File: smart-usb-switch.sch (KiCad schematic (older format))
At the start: 8 parts, among them J1 USB_A, J2 USB_A, J3 Conn_01x04, J4 Conn_01x02, Q1 2N7002E, U1 ESP-12F, U2 TLV75533PDBV

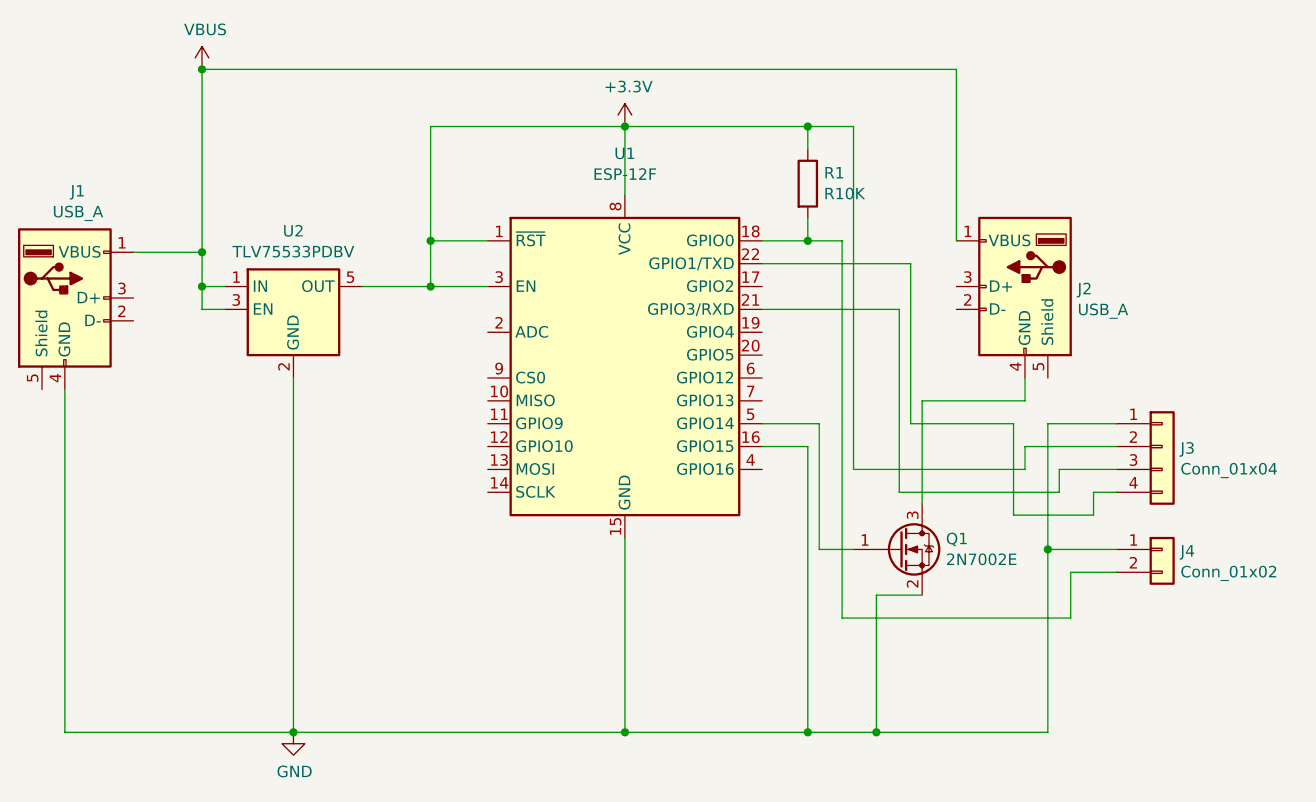
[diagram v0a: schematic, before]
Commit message: Fix #1: switch to GPIO4
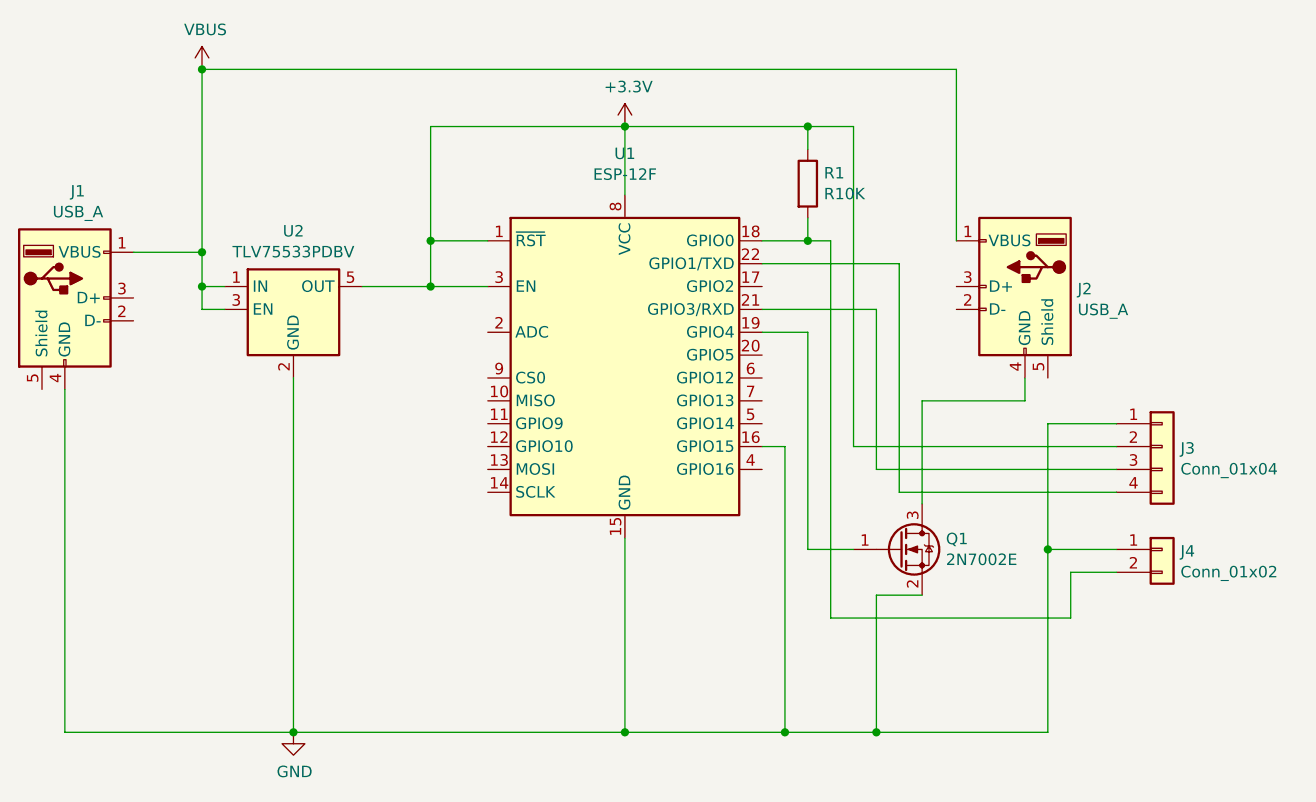
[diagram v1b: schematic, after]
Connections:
- net at U1.19 (GPIO4): now also Q1.1 (G)
- net at U1.5 (GPIO14): no longer Q1.1 (G)
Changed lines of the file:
@@
 EESchema Schematic File Version 4
-EELAYER 30 0
+EELAYER 26 0
 EELAYER END
 $Descr A4 11693 8268
@@
 Connection ~ 6800 4750
 Wire Wire Line
-	6800 4750 6500 4750
+	6800 4750 6400 4750
 Wire Wire Line
 	6800 4750 7550 4750
@@
 $EndComp
 Wire Wire Line
-	6950 3400 6950 2700
-Wire Wire Line
-	6950 2700 6300 2700
-Wire Wire Line
-	6300 2900 6900 2900
-Wire Wire Line
-	6700 3600 6700 2100
+	6900 3700 6900 2700
+Wire Wire Line
+	6900 2700 6300 2700
+Wire Wire Line
+	6300 2900 6800 2900
 Wire Wire Line
 	6700 2100 6500 2100
@@
 	7550 3400 7550 3950
 Wire Wire Line
-	7850 3500 7450 3500
-Wire Wire Line
-	7450 3500 7450 3600
-Wire Wire Line
-	7450 3600 6700 3600
-Wire Wire Line
-	7850 3600 7600 3600
-Wire Wire Line
-	7600 3600 7600 3700
-Wire Wire Line
-	7600 3700 6900 3700
-Wire Wire Line
-	6900 2900 6900 3700
-Wire Wire Line
-	6950 3400 7400 3400
-Wire Wire Line
-	7400 3400 7400 3800
-Wire Wire Line
-	7400 3800 7750 3800
-Wire Wire Line
-	7750 3800 7750 3700
-Wire Wire Line
-	7750 3700 7850 3700
+	6800 2900 6800 3600
 $Comp
 L Connector_Generic:Conn_01x02 J4
@@
 	6300 2600 6500 2600
 Wire Wire Line
-	6650 2600 6650 4250
+	6600 2600 6600 4250
 Wire Wire Line
 	7850 4050 7650 4050
 Wire Wire Line
-	6700 3950 6550 3950
-Wire Wire Line
-	6650 4250 7650 4250
+	6700 3950 6500 3950
+Wire Wire Line
+	6600 4250 7650 4250
 Wire Wire Line
 	7650 4250 7650 4050
@@
 	4250 3200 4250 4750
 Connection ~ 4250 4750
-Wire Wire Line
-	6550 3950 6550 3400
-Wire Wire Line
-	6550 3400 6300 3400
 $Comp
 L Transistor_FET:2N7002E Q1
@@
 	4850 2600 4850 2100
 Wire Wire Line
-	6300 3500 6500 3500
-Wire Wire Line
-	6500 3500 6500 4750
-Connection ~ 6500 4750
-Wire Wire Line
-	6500 4750 5700 4750
+	6300 3500 6400 3500
+Wire Wire Line
+	6400 3500 6400 4750
+Connection ~ 6400 4750
+Wire Wire Line
+	6400 4750 5700 4750
 $Comp
 L Device:R R1
@@
 Connection ~ 6500 2600
 Wire Wire Line
-	6500 2600 6650 2600
+	6500 2600 6600 2600
 Wire Wire Line
 	6500 2200 6500 2100
@@
 Wire Wire Line
 	7000 3300 7450 3300
+Wire Wire Line
+	6500 3000 6300 3000
+Wire Wire Line
+	6500 3000 6500 3950
+Wire Wire Line
+	6700 3500 6700 2100
+Wire Wire Line
+	6700 3500 7850 3500
+Wire Wire Line
+	6800 3600 7850 3600
+Wire Wire Line
+	6900 3700 7850 3700
 $EndSCHEMATC

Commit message: more docs, updates
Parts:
- U2: symbol Regulator_Linear:TLV75533PDBV -> smart-usb-switch-rescue:TLV75533PDBV-Regulator_Linear
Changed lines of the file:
@@
 EESchema Schematic File Version 4
-EELAYER 26 0
+EELAYER 30 0
 EELAYER END
 $Descr A4 11693 8268
@@
 	5700 2100 5700 2400
 $Comp
-L Regulator_Linear:TLV75533PDBV U2
+L smart-usb-switch-rescue:TLV75533PDBV-Regulator_Linear U2
 U 1 1 5DE30043
 P 4250 2900

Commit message: reroute
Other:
- moved on the sheet: J2, Q1
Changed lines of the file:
@@
 $EndComp
 Wire Wire Line
-	3250 4750 4250 4750
-Wire Wire Line
-	5700 4750 5700 3900
+	5700 4050 5700 3900
 Wire Wire Line
 	3550 2650 3850 2650
@@
 L Connector:USB_A J2
 U 1 1 5DE34A4B
-P 7450 2800
-F 0 "J2" H 7220 2789 50  0000 R CNN
-F 1 "USB_A" H 7220 2698 50  0000 R CNN
-F 2 "Connector_USB:USB_A_Stewart_SS-52100-001_Horizontal" H 7600 2750 50  0001 C CNN
-F 3 " ~" H 7600 2750 50  0001 C CNN
-	1    7450 2800
+P 7600 2050
+F 0 "J2" H 7370 2039 50  0000 R CNN
+F 1 "USB_A" H 7370 1948 50  0000 R CNN
+F 2 "Connector_USB:USB_A_Stewart_SS-52100-001_Horizontal" H 7750 2000 50  0001 C CNN
+F 3 " ~" H 7750 2000 50  0001 C CNN
+	1    7600 2050
 	-1   0    0    -1
 $EndComp
-Wire Wire Line
-	7450 3200 7450 3300
-Connection ~ 5700 4750
-Wire Wire Line
-	6800 4150 6800 4750
-Connection ~ 6800 4750
-Wire Wire Line
-	6800 4750 6400 4750
-Wire Wire Line
-	6800 4750 7550 4750
+Connection ~ 5700 4050
 $Comp
 L power:GND #PWR0101
 U 1 1 5DE35A33
-P 4250 4750
-F 0 "#PWR0101" H 4250 4500 50  0001 C CNN
-F 1 "GND" H 4255 4577 50  0000 C CNN
-F 2 "" H 4250 4750 50  0001 C CNN
-F 3 "" H 4250 4750 50  0001 C CNN
-	1    4250 4750
+P 4250 3400
+F 0 "#PWR0101" H 4250 3150 50  0001 C CNN
+F 1 "GND" H 4255 3227 50  0000 C CNN
+F 2 "" H 4250 3400 50  0001 C CNN
+F 3 "" H 4250 3400 50  0001 C CNN
+	1    4250 3400
 	1    0    0    -1
 $EndComp
@@
 Connection ~ 5700 2100
 Wire Wire Line
-	7150 2600 7150 1850
-Wire Wire Line
-	7150 1850 3850 1850
-Wire Wire Line
 	3850 1850 3850 2650
 Connection ~ 3850 2650
-Wire Wire Line
-	6800 4150 7000 4150
 $Comp
 L Connector_Generic:Conn_01x04 J3
@@
 	6700 2100 6500 2100
 Wire Wire Line
-	7850 3400 7550 3400
-Wire Wire Line
-	7550 3400 7550 3950
-Wire Wire Line
 	6800 2900 6800 3600
 $Comp
@@
 	6300 2600 6500 2600
 Wire Wire Line
-	6600 2600 6600 4250
-Wire Wire Line
-	7850 4050 7650 4050
-Wire Wire Line
-	6700 3950 6500 3950
-Wire Wire Line
-	6600 4250 7650 4250
-Wire Wire Line
-	7650 4250 7650 4050
-Wire Wire Line
-	7550 3950 7850 3950
-Connection ~ 7550 3950
-Wire Wire Line
-	7550 3950 7550 4750
-Wire Wire Line
-	4250 3200 4250 4750
-Connection ~ 4250 4750
+	6600 2600 6600 4050
+Wire Wire Line
+	7350 3950 7850 3950
+Wire Wire Line
+	4250 3200 4250 3400
 $Comp
 L Transistor_FET:2N7002E Q1
 U 1 1 5DE386B7
-P 6900 3950
-F 0 "Q1" H 7104 3996 50  0000 L CNN
-F 1 "2N7002E" H 7104 3905 50  0000 L CNN
-F 2 "Package_TO_SOT_SMD:SOT-23" H 7100 3875 50  0001 L CIN
-F 3 "http://www.diodes.com/assets/Datasheets/ds30376.pdf" H 6900 3950 50  0001 L CNN
-	1    6900 3950
+P 7250 3000
+F 0 "Q1" H 7454 3046 50  0000 L CNN
+F 1 "2N7002E" H 7454 2955 50  0000 L CNN
+F 2 "Package_TO_SOT_SMD:SOT-23" H 7450 2925 50  0001 L CIN
+F 3 "http://www.diodes.com/assets/Datasheets/ds30376.pdf" H 7250 3000 50  0001 L CNN
+	1    7250 3000
 	1    0    0    -1
 $EndComp
@@
 	6300 3500 6400 3500
 Wire Wire Line
-	6400 3500 6400 4750
-Connection ~ 6400 4750
-Wire Wire Line
-	6400 4750 5700 4750
+	6400 3500 6400 4050
+Wire Wire Line
+	6400 4050 5700 4050
 $Comp
 L Device:R R1
@@
 Connection ~ 3850 1850
 Wire Wire Line
-	4250 4750 5700 4750
-Wire Wire Line
-	3250 3250 3250 4750
-Wire Wire Line
-	7000 3750 7000 3300
-Wire Wire Line
-	7000 3300 7450 3300
-Wire Wire Line
-	6500 3000 6300 3000
-Wire Wire Line
-	6500 3000 6500 3950
+	3250 3250 3250 3400
+Wire Wire Line
+	7350 2800 7350 2450
+Wire Wire Line
+	7350 2450 7600 2450
 Wire Wire Line
 	6700 3500 6700 2100
@@
 Wire Wire Line
 	6900 3700 7850 3700
+$Comp
+L power:GND #PWR?
+U 1 1 5DF189E7
+P 3250 3400
+F 0 "#PWR?" H 3250 3150 50  0001 C CNN
+F 1 "GND" H 3255 3227 50  0000 C CNN
+F 2 "" H 3250 3400 50  0001 C CNN
+F 3 "" H 3250 3400 50  0001 C CNN
+	1    3250 3400
+	1    0    0    -1
+$EndComp
+$Comp
+L power:GND #PWR?
+U 1 1 5DF18E62
+P 5700 4050
+F 0 "#PWR?" H 5700 3800 50  0001 C CNN
+F 1 "GND" H 5705 3877 50  0000 C CNN
+F 2 "" H 5700 4050 50  0001 C CNN
+F 3 "" H 5700 4050 50  0001 C CNN
+	1    5700 4050
+	1    0    0    -1
+$EndComp
+$Comp
+L power:GND #PWR?
+U 1 1 5DF19647
+P 7350 4150
+F 0 "#PWR?" H 7350 3900 50  0001 C CNN
+F 1 "GND" H 7355 3977 50  0000 C CNN
+F 2 "" H 7350 4150 50  0001 C CNN
+F 3 "" H 7350 4150 50  0001 C CNN
+	1    7350 4150
+	1    0    0    -1
+$EndComp
+Wire Wire Line
+	3850 1850 7300 1850
+Wire Wire Line
+	6600 4050 7850 4050
+Wire Wire Line
+	6300 3000 7050 3000
+Wire Wire Line
+	7350 3200 7350 3400
+Connection ~ 7350 3400
+Wire Wire Line
+	7350 3400 7350 3950
+Wire Wire Line
+	7350 3400 7850 3400
+Connection ~ 7350 3950
+Wire Wire Line
+	7350 3950 7350 4150
 $EndSCHEMATC

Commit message: update components to standard library
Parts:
- Q1: value 2N7002E -> DMN6140L-13; symbol Transistor_FET:2N7002E -> Transistor_FET:2N7002
- U2: symbol smart-usb-switch-rescue:TLV75533PDBV-Regulator_Linear -> Regulator_Linear:TLV75533PDBV
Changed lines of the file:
@@
 	5700 2100 5700 2400
 $Comp
-L smart-usb-switch-rescue:TLV75533PDBV-Regulator_Linear U2
+L Regulator_Linear:TLV75533PDBV U2
 U 1 1 5DE30043
 P 4250 2900
@@
 	4250 3200 4250 3400
 $Comp
-L Transistor_FET:2N7002E Q1
+L Transistor_FET:2N7002 Q1
 U 1 1 5DE386B7
 P 7250 3000
 F 0 "Q1" H 7454 3046 50  0000 L CNN
-F 1 "2N7002E" H 7454 2955 50  0000 L CNN
+F 1 "DMN6140L-13" H 7454 2955 50  0000 L CNN
 F 2 "Package_TO_SOT_SMD:SOT-23" H 7450 2925 50  0001 L CIN
-F 3 "http://www.diodes.com/assets/Datasheets/ds30376.pdf" H 7250 3000 50  0001 L CNN
+F 3 "https://www.mouser.com/datasheet/2/115/DMN6140L-477770.pdfx" H 7250 3000 50  0001 L CNN
 	1    7250 3000
 	1    0    0    -1

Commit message: Add buttons. Reroute, improve docs
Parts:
- added SW1, SW2: SW_Push, Button_Switch_SMD:SW_SPST_SKQG_WithStem, symbol Switch:SW_Push
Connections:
- net GND: now also SW1.2, SW2.2
- net at U1.6 (GPIO12): now also SW1.1
- net at U1.7 (GPIO13): now also SW2.1
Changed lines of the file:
@@
 F 1 "DMN6140L-13" H 7454 2955 50  0000 L CNN
 F 2 "Package_TO_SOT_SMD:SOT-23" H 7450 2925 50  0001 L CIN
-F 3 "https://www.mouser.com/datasheet/2/115/DMN6140L-477770.pdfx" H 7250 3000 50  0001 L CNN
+F 3 "https://www.mouser.com/datasheet/2/115/DMN6140L-477770.pdf" H 7250 3000 50  0001 L CNN
 	1    7250 3000
 	1    0    0    -1
@@
 	6900 3700 7850 3700
 $Comp
-L power:GND #PWR?
+L power:GND #PWR0104
 U 1 1 5DF189E7
 P 3250 3400
-F 0 "#PWR?" H 3250 3150 50  0001 C CNN
+F 0 "#PWR0104" H 3250 3150 50  0001 C CNN
 F 1 "GND" H 3255 3227 50  0000 C CNN
 F 2 "" H 3250 3400 50  0001 C CNN
@@
 $EndComp
 $Comp
-L power:GND #PWR?
+L power:GND #PWR0105
 U 1 1 5DF18E62
 P 5700 4050
-F 0 "#PWR?" H 5700 3800 50  0001 C CNN
+F 0 "#PWR0105" H 5700 3800 50  0001 C CNN
 F 1 "GND" H 5705 3877 50  0000 C CNN
 F 2 "" H 5700 4050 50  0001 C CNN
@@
 $EndComp
 $Comp
-L power:GND #PWR?
+L power:GND #PWR0106
 U 1 1 5DF19647
 P 7350 4150
-F 0 "#PWR?" H 7350 3900 50  0001 C CNN
+F 0 "#PWR0106" H 7350 3900 50  0001 C CNN
 F 1 "GND" H 7355 3977 50  0000 C CNN
 F 2 "" H 7350 4150 50  0001 C CNN
@@
 Wire Wire Line
 	7350 3950 7350 4150
+$Comp
+L Switch:SW_Push SW1
+U 1 1 5E15846A
+P 3850 3900
+F 0 "SW1" H 3850 4185 50  0000 C CNN
+F 1 "SW_Push" H 3850 4094 50  0000 C CNN
+F 2 "Button_Switch_SMD:SW_SPST_SKQG_WithStem" H 3850 4100 50  0001 C CNN
+F 3 "" H 3850 4100 50  0001 C CNN
+	1    3850 3900
+	1    0    0    -1
+$EndComp
+$Comp
+L Switch:SW_Push SW2
+U 1 1 5E158E27
+P 3850 4350
+F 0 "SW2" H 3850 4635 50  0000 C CNN
+F 1 "SW_Push" H 3850 4544 50  0000 C CNN
+F 2 "Button_Switch_SMD:SW_SPST_SKQG_WithStem" H 3850 4550 50  0001 C CNN
+F 3 "" H 3850 4550 50  0001 C CNN
+	1    3850 4350
+	1    0    0    -1
+$EndComp
+Wire Wire Line
+	4050 3900 4750 3900
+Wire Wire Line
+	4750 3900 4750 4050
+Wire Wire Line
+	4750 4050 5700 4050
+Wire Wire Line
+	4050 4350 4750 4350
+Wire Wire Line
+	4750 4350 4750 4050
+Connection ~ 4750 4050
+Wire Wire Line
+	7000 3200 7000 4550
+Wire Wire Line
+	7000 4550 3450 4550
+Wire Wire Line
+	3450 4550 3450 3900
+Wire Wire Line
+	3450 3900 3650 3900
+Wire Wire Line
+	6300 3200 7000 3200
+Wire Wire Line
+	7100 3300 7100 4650
+Wire Wire Line
+	7100 4650 3550 4650
+Wire Wire Line
+	3550 4650 3550 4350
+Wire Wire Line
+	3550 4350 3650 4350
+Wire Wire Line
+	6300 3300 7100 3300
 $EndSCHEMATC

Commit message: Add machine-readable BOM and LCSC part numbers
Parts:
- Q1: LCSC (none) -> C211403
- R1: LCSC (none) -> C17414
- SW1, SW2: LCSC (none) -> C318888
- U2: symbol Regulator_Linear:TLV75533PDBV -> smart-usb-switch-rescue:TLV75533PDBV-Regulator_Linear; LCSC (none) -> C404027
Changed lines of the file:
@@
 	5700 2100 5700 2400
 $Comp
-L Regulator_Linear:TLV75533PDBV U2
+L smart-usb-switch-rescue:TLV75533PDBV-Regulator_Linear U2
 U 1 1 5DE30043
 P 4250 2900
@@
 F 2 "Package_TO_SOT_SMD:SOT-23-5" H 4250 3225 50  0001 C CIN
 F 3 "http://www.ti.com/lit/ds/symlink/tlv755p.pdf" H 4250 2950 50  0001 C CNN
+F 4 "C404027" H 4250 2900 50  0001 C CNN "LCSC"
 	1    4250 2900
 	1    0    0    -1
@@
 F 2 "Package_TO_SOT_SMD:SOT-23" H 7450 2925 50  0001 L CIN
 F 3 "https://www.mouser.com/datasheet/2/115/DMN6140L-477770.pdf" H 7250 3000 50  0001 L CNN
+F 4 "C211403" H 7250 3000 50  0001 C CNN "LCSC"
 	1    7250 3000
 	1    0    0    -1
@@
 F 2 "Resistor_SMD:R_0805_2012Metric" V 6430 2350 50  0001 C CNN
 F 3 "~" H 6500 2350 50  0001 C CNN
+F 4 "C17414" H 6500 2350 50  0001 C CNN "LCSC"
 	1    6500 2350
 	1    0    0    -1
@@
 F 2 "Button_Switch_SMD:SW_SPST_SKQG_WithStem" H 3850 4100 50  0001 C CNN
 F 3 "" H 3850 4100 50  0001 C CNN
+F 4 "C318888" H 3850 3900 50  0001 C CNN "LCSC"
 	1    3850 3900
 	1    0    0    -1
@@
 F 2 "Button_Switch_SMD:SW_SPST_SKQG_WithStem" H 3850 4550 50  0001 C CNN
 F 3 "" H 3850 4550 50  0001 C CNN
+F 4 "C318888" H 3850 4350 50  0001 C CNN "LCSC"
 	1    3850 4350
 	1    0    0    -1

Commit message: More LCSC and docs
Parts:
- J1: LCSC (none) -> C46394
- J2: LCSC (none) -> C86461
- U1: LCSC (none) -> C82891
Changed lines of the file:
@@
 F 2 "RF_Module:ESP-12E" H 5700 3200 50  0001 C CNN
 F 3 "http://wiki.ai-thinker.com/_media/esp8266/esp8266_series_modules_user_manual_v1.1.pdf" H 5350 3300 50  0001 C CNN
+F 4 "C82891" H 5700 3200 50  0001 C CNN "LCSC"
 	1    5700 3200
 	1    0    0    -1
@@
 F 2 "Connector_USB:USB_A_CNCTech_1001-011-01101_Horizontal" H 3400 2800 50  0001 C CNN
 F 3 " ~" H 3400 2800 50  0001 C CNN
+F 4 "C46394" H 3250 2850 50  0001 C CNN "LCSC"
 	1    3250 2850
 	1    0    0    -1
@@
 F 2 "Connector_USB:USB_A_Stewart_SS-52100-001_Horizontal" H 7750 2000 50  0001 C CNN
 F 3 " ~" H 7750 2000 50  0001 C CNN
+F 4 "C86461" H 7600 2050 50  0001 C CNN "LCSC"
 	1    7600 2050
 	-1   0    0    -1

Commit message: JLCPCB mfg
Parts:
- U2: value TLV75533PDBV -> MIC5219-3.3YM5-TR; symbol smart-usb-switch-rescue:TLV75533PDBV-Regulator_Linear -> Regulator_Linear:MIC5219-3.3YM5; LCSC C404027 -> C29613
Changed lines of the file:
@@
 F 1 "USB_A" H 3307 3226 50  0000 C CNN
 F 2 "Connector_USB:USB_A_CNCTech_1001-011-01101_Horizontal" H 3400 2800 50  0001 C CNN
-F 3 " ~" H 3400 2800 50  0001 C CNN
+F 3 "https://datasheet.lcsc.com/szlcsc/1811131821_Jing-Extension-of-the-Electronic-Co-C46394_C46394.pdf" H 3400 2800 50  0001 C CNN
 F 4 "C46394" H 3250 2850 50  0001 C CNN "LCSC"
 	1    3250 2850
@@
 	5700 2100 5700 2400
 $Comp
-L smart-usb-switch-rescue:TLV75533PDBV-Regulator_Linear U2
+L Regulator_Linear:MIC5219-3.3YM5 U2
 U 1 1 5DE30043
 P 4250 2900
 F 0 "U2" H 4250 3242 50  0000 C CNN
-F 1 "TLV75533PDBV" H 4250 3151 50  0000 C CNN
+F 1 "MIC5219-3.3YM5-TR" H 4250 3151 50  0000 C CNN
 F 2 "Package_TO_SOT_SMD:SOT-23-5" H 4250 3225 50  0001 C CIN
-F 3 "http://www.ti.com/lit/ds/symlink/tlv755p.pdf" H 4250 2950 50  0001 C CNN
-F 4 "C404027" H 4250 2900 50  0001 C CNN "LCSC"
+F 3 "http://ww1.microchip.com/downloads/en/DeviceDoc/MIC5219-500mA-Peak-Output-LDO-Regulator-DS20006021A.pdf" H 4250 2950 50  0001 C CNN
+F 4 "C29613" H 4250 2900 50  0001 C CNN "LCSC"
 	1    4250 2900
 	1    0    0    -1
@@
 F 1 "USB_A" H 7370 1948 50  0000 R CNN
 F 2 "Connector_USB:USB_A_Stewart_SS-52100-001_Horizontal" H 7750 2000 50  0001 C CNN
-F 3 " ~" H 7750 2000 50  0001 C CNN
+F 3 "https://datasheet.lcsc.com/szlcsc/1811131820_TE-Connectivity-292303-1_C86461.pdf" H 7750 2000 50  0001 C CNN
 F 4 "C86461" H 7600 2050 50  0001 C CNN "LCSC"
 	1    7600 2050
@@
 F 1 "SW_Push" H 3850 4094 50  0000 C CNN
 F 2 "Button_Switch_SMD:SW_SPST_SKQG_WithStem" H 3850 4100 50  0001 C CNN
-F 3 "" H 3850 4100 50  0001 C CNN
+F 3 "https://datasheet.lcsc.com/szlcsc/1810291657_XKB-Enterprise-TS-1187A-C-D-B_C318888.pdf" H 3850 4100 50  0001 C CNN
 F 4 "C318888" H 3850 3900 50  0001 C CNN "LCSC"
 	1    3850 3900
@@
 F 1 "SW_Push" H 3850 4544 50  0000 C CNN
 F 2 "Button_Switch_SMD:SW_SPST_SKQG_WithStem" H 3850 4550 50  0001 C CNN
-F 3 "" H 3850 4550 50  0001 C CNN
+F 3 "https://datasheet.lcsc.com/szlcsc/1810291657_XKB-Enterprise-TS-1187A-C-D-B_C318888.pdf" H 3850 4550 50  0001 C CNN
 F 4 "C318888" H 3850 4350 50  0001 C CNN "LCSC"
 	1    3850 4350
